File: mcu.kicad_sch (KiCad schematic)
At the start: 42 parts, among them J12 USB_C_Receptacle_USB2.0_16P, J13 MSD-11-A, U4 ESP32-S3-WROOM-1, U5 STM32C011F4Ux, Y1 Crystal_GND24

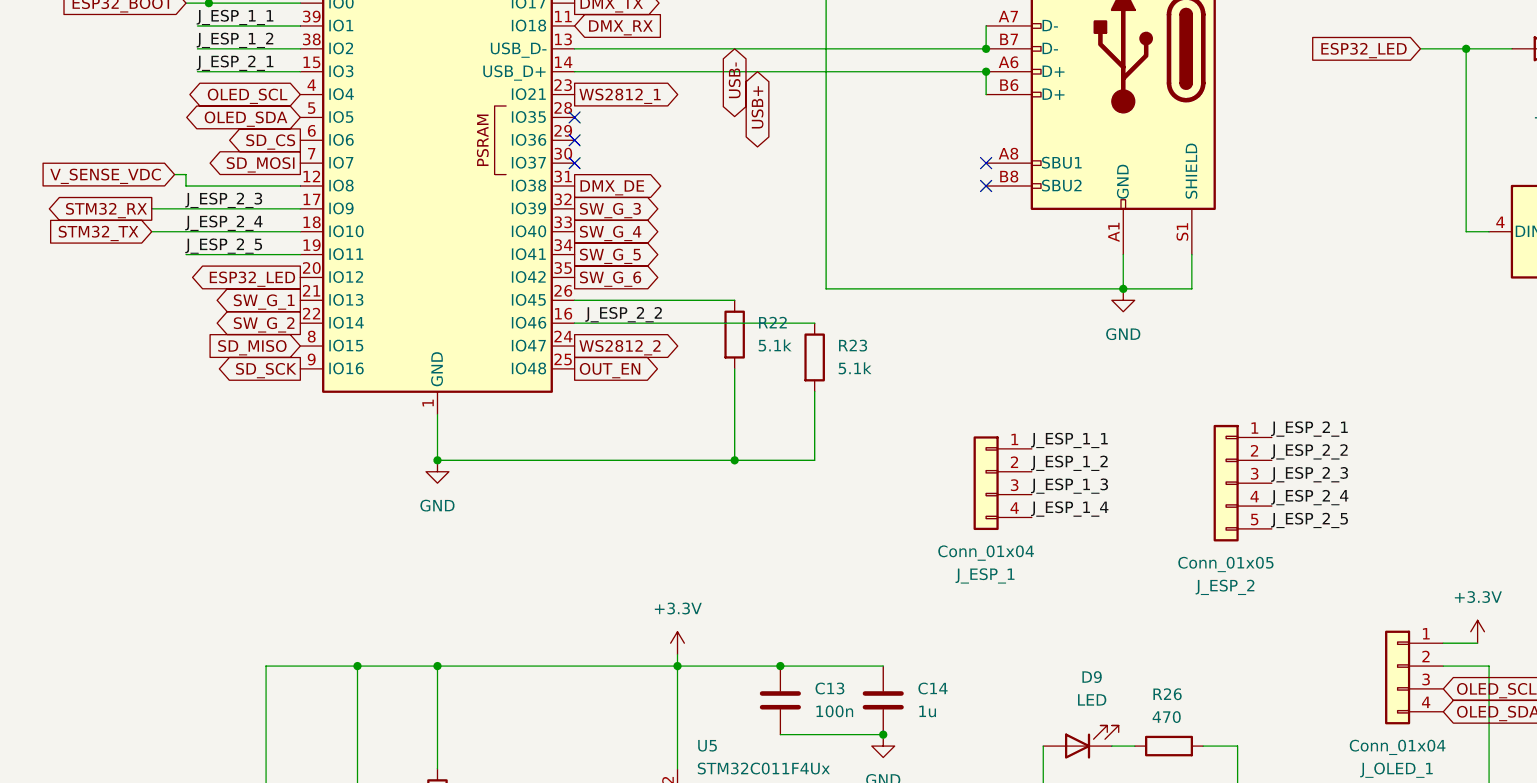
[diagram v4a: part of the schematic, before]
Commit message: schematic changes for mini
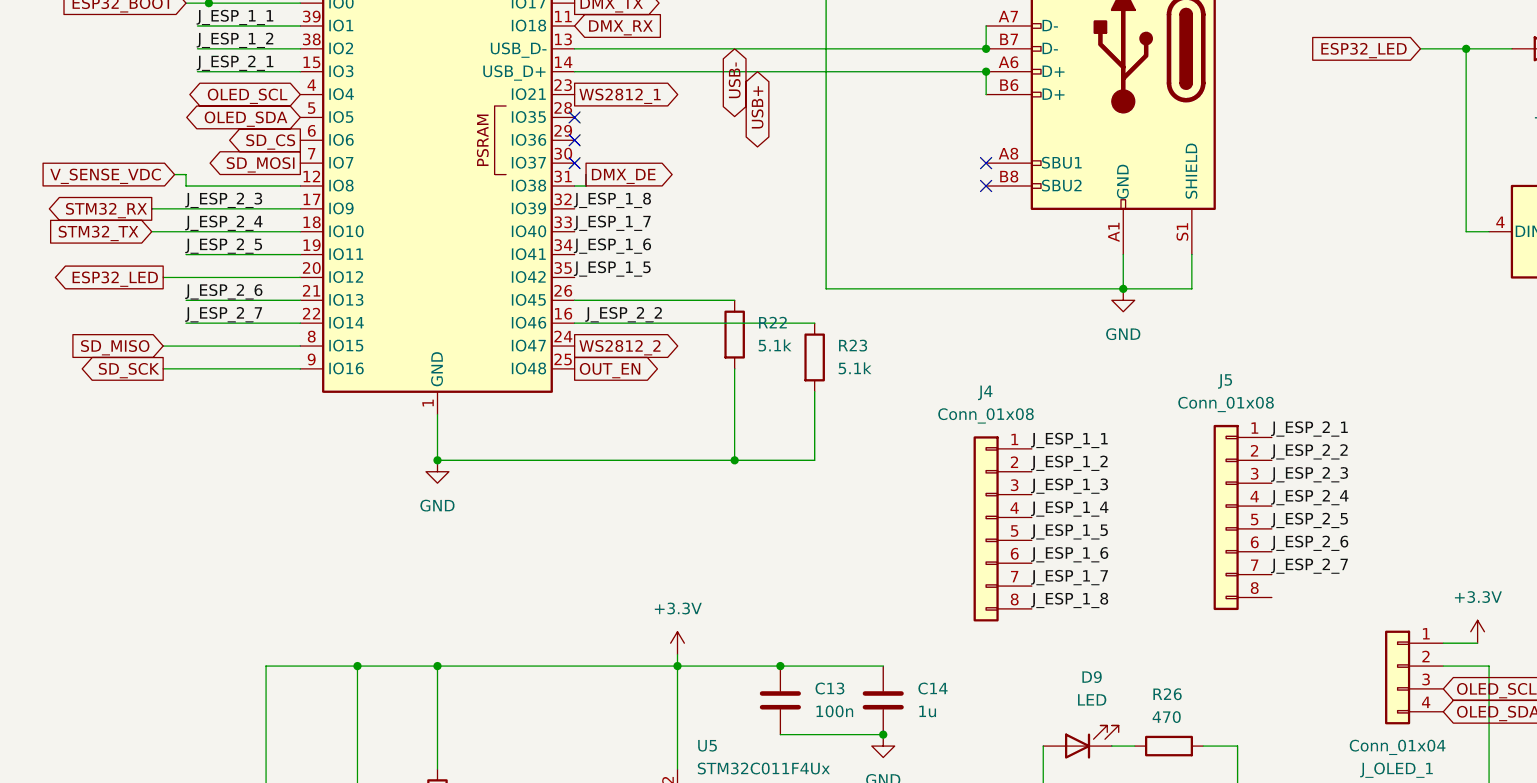
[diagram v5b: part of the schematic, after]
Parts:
- removed J_ESP_1: Conn_01x04, Connector_PinHeader_2.54mm:PinHeader_1x04_P2.54mm_Vertical, symbol Connector_Generic:Conn_01x04
- removed J_ESP_2: Conn_01x05, Connector_PinSocket_2.54mm:PinSocket_1x05_P2.54mm_Vertical, symbol Connector_Generic:Conn_01x05
- added J4, J5: Conn_01x08, Connector_PinSocket_2.54mm:PinSocket_1x08_P2.54mm_Vertical, symbol Connector_Generic:Conn_01x08
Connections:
- net J_ESP_1_1: now also J4.1 (Pin_1)
- net J_ESP_1_2: now also J4.2 (Pin_2)
- net J_ESP_1_3: now also J4.3 (Pin_3)
- net J_ESP_1_4: now also J4.4 (Pin_4)
- net J_ESP_2_1: now also J5.1 (Pin_1)
- net J_ESP_2_2: now also J5.2 (Pin_2)
- net J_ESP_2_5: now also J5.5 (Pin_5)
- net STM32_RX: now also J5.3 (Pin_3)
- net STM32_TX: now also J5.4 (Pin_4)
- net SW_G_1 renamed J_ESP_2_6
- net J_ESP_2_6: now also J5.6 (Pin_6)
- net SW_G_2 renamed J_ESP_2_7
- net J_ESP_2_7: now also J5.7 (Pin_7)
- net SW_G_3 renamed J_ESP_1_8
- net J_ESP_1_8: now also J4.8 (Pin_8)
- net SW_G_4 renamed J_ESP_1_7
- net J_ESP_1_7: now also J4.7 (Pin_7)
- net SW_G_5 renamed J_ESP_1_6
- net J_ESP_1_6: now also J4.6 (Pin_6)
- net SW_G_6 renamed J_ESP_1_5
- net J_ESP_1_5: now also J4.5 (Pin_5)

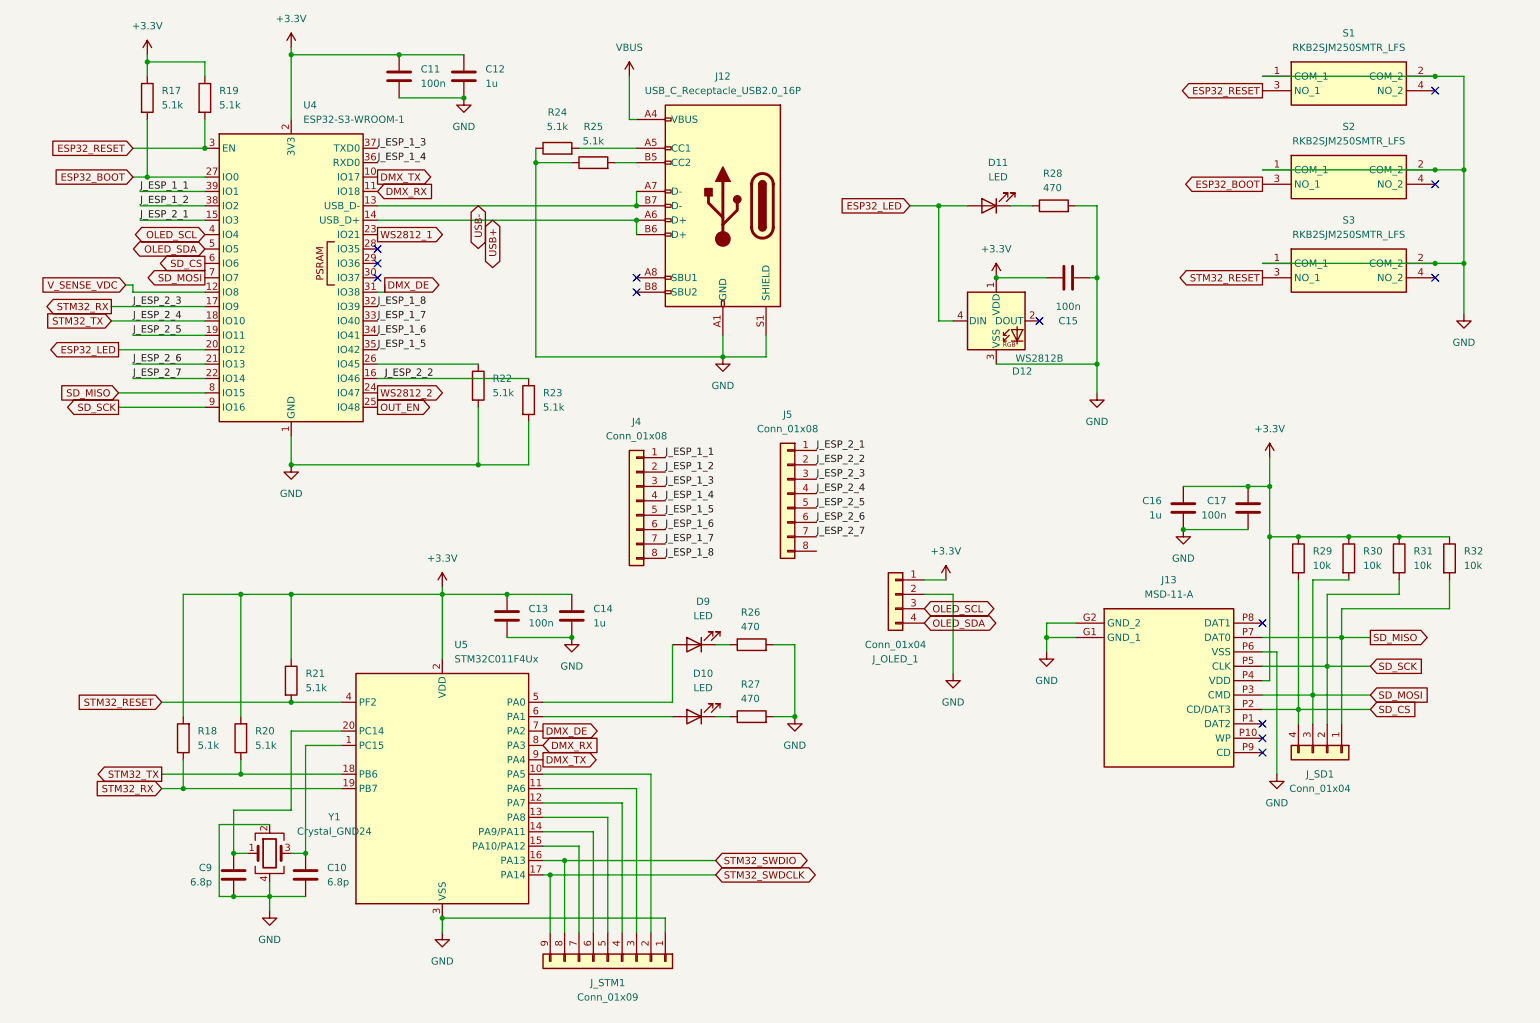
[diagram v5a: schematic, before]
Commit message: complete top layer layout
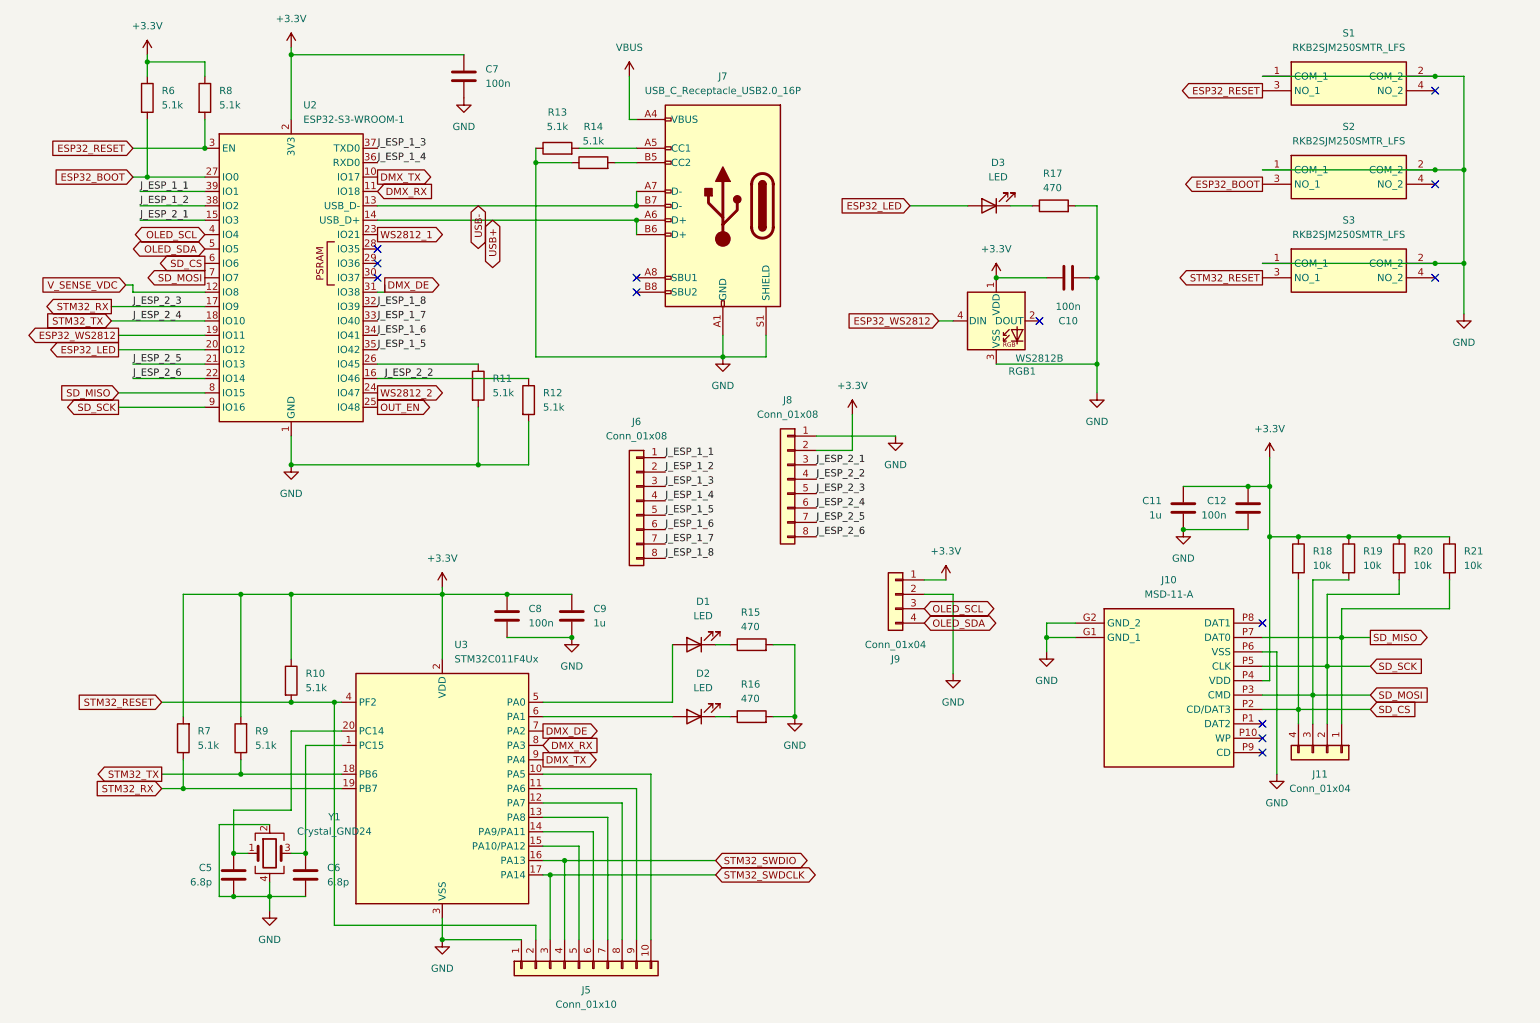
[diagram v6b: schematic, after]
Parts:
- removed C12: 1u, Capacitor_SMD:C_0603_1608Metric_Pad1.08x0.95mm_HandSolder, symbol Device:C
- removed J_STM1: Conn_01x09, Connector_PinHeader_2.54mm:PinHeader_1x09_P2.54mm_Vertical, symbol Connector_Generic:Conn_01x09
- added J5: Conn_01x10, Connector_PinHeader_2.54mm:PinHeader_1x10_P2.54mm_Vertical, symbol Connector_Generic:Conn_01x10
- renumbered C15 to C10, C16 to C11, C17 to C12, C9 to C5, C10 to C6, C11 to C7, C13 to C8, C14 to C9, D9 to D1, D10 to D2, D11 to D3, J13 to J10, J_SD1 to J11, J4 to J6, J12 to J7, J5 to J8, J_OLED_1 to J9, R21 to R10, R22 to R11, R23 to R12, R24 to R13, R25 to R14, R26 to R15, R27 to R16, R28 to R17, R29 to R18, R30 to R19, R31 to R20, R32 to R21, R17 to R6, R18 to R7, R19 to R8, R20 to R9, D12 to RGB1, U4 to U2, U5 to U3
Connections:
- net +3.3V: now also J8.2 (Pin_2)
- net ESP32_LED: no longer RGB1.4 (DIN)
- net GND: now also J8.1 (Pin_1), J5.1 (Pin_1)
- net J_ESP_2_1: now also J8.3 (Pin_3); no longer J8.1 (Pin_1)
- net J_ESP_2_2: now also J8.4 (Pin_4); no longer J8.2 (Pin_2)
- net J_ESP_2_5: now also J8.7 (Pin_7), U2.21 (IO13); no longer J8.5 (Pin_5), U2.19 (IO11)
- net J_ESP_2_6: now also J8.8 (Pin_8), U2.22 (IO14); no longer J8.6 (Pin_6), U2.21 (IO13)
- net STM32_RESET: now also J5.2 (Pin_2)
- net STM32_RX: now also J8.5 (Pin_5); no longer J8.3 (Pin_3)
- net STM32_SWDCLK: now also J5.3 (Pin_3)
- net STM32_SWDIO: now also J5.4 (Pin_4)
- net STM32_TX: now also J8.6 (Pin_6); no longer J8.4 (Pin_4)
- net at U3.10 (PA5): now also J5.10 (Pin_10)
- net at U3.11 (PA6): now also J5.9 (Pin_9)
- net at U3.12 (PA7): now also J5.8 (Pin_8)
- net at U3.13 (PA8): now also J5.7 (Pin_7)
- net at U3.14 (PA9/PA11): now also J5.6 (Pin_6)
- net at U3.15 (PA10/PA12): now also J5.5 (Pin_5)
- removed net J_ESP_2_7: J8.7 (Pin_7), U2.22 (IO14)
- new net ESP32_WS2812: RGB1.4 (DIN), U2.19 (IO11)
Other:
- moved on the sheet: C7, J8

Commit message: complete layout, routing, and silkscreen
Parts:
- removed C11: 1u, Capacitor_SMD:C_0603_1608Metric_Pad1.08x0.95mm_HandSolder, symbol Device:C
- J6, J8: footprint Connector_PinSocket_2.54mm:PinSocket_1x08_P2.54mm_Vertical -> Connector_PinHeader_2.54mm:PinHeader_1x08_P2.54mm_Vertical
- R18, R19, R20, R21: value 10k -> 470
- renumbered C12 to C11
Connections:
- net +3.3V: no longer R18.1, R19.1, R20.1, R21.1
- net SD_CS: now also R21.2; no longer J10.P2 (CD/DAT3), R18.2
- net SD_MISO: now also R18.2, U2.9 (IO16); no longer J10.P7 (DAT0), R21.2, U2.8 (IO15)
- net SD_MOSI: no longer J10.P3 (CMD)
- net SD_SCK: now also U2.8 (IO15); no longer J10.P5 (CLK), U2.9 (IO16)
- new net: J10.P2 (CD/DAT3), R21.1
- new net: J10.P3 (CMD), R19.1
- new net: J10.P5 (CLK), R20.1
- new net: J10.P7 (DAT0), R18.1
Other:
- moved on the sheet: C11, J11
